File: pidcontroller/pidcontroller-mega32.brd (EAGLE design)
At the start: 100 x 75.4 mm, 26 parts, among them IC2 MAX3232CWE, IC3 MEGA32-A

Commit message: updated board
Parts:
- added BTNDN, BTNOK, BTNUP: (no value), wirepad:2,15/1,0
- added R4, R5, R6: (no value), resistor:R0603
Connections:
- new net BTNDN: BTNDN.1, IC3.12, R5.1
- new net BTNOK: BTNOK.1, IC3.11, R6.1
- new net BTNUP: BTNUP.1, IC3.13, R4.1
- net GND: now also R4.2, R5.2, R6.2
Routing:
- net BTNUP: track 0.00 -> 24.9 mm
- net BTNDN: track 0.00 -> 20.1 mm
- net BTNOK: track 0.00 -> 16.1 mm
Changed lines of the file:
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@@
 <?xml version="1.0" encoding="utf-8"?>
 <!DOCTYPE eagle SYSTEM "eagle.dtd">
-<eagle version="6.4">
+<eagle version="6.5.0">
 <drawing>
 <settings>
@@
 <element name="JP6" library="pinhead" package="1X01" value="" x="21" y="11"/>
 <element name="JP7" library="pinhead" package="1X01" value="" x="21" y="17"/>
+<element name="BTNUP" library="wirepad" package="2,15/1,0" value="" x="39" y="24"/>
+<element name="BTNDN" library="wirepad" package="2,15/1,0" value="" x="39" y="28"/>
+<element name="BTNOK" library="wirepad" package="2,15/1,0" value="" x="39" y="32"/>
+<element name="R4" library="resistor" package="R0603" value="" x="34" y="24" rot="R180"/>
+<element name="R5" library="resistor" package="R0603" value="" x="34" y="28" rot="R180"/>
+<element name="R6" library="resistor" package="R0603" value="" x="34" y="32" rot="R180"/>
 </elements>
 <signals>
@@
 <vertex x="100" y="75"/>
 </polygon>
+<contactref element="R6" pad="2"/>
+<contactref element="R5" pad="2"/>
+<contactref element="R4" pad="2"/>
 </signal>
 <signal name="N$9">
@@
 <contactref element="IC3" pad="14"/>
 <contactref element="R1" pad="2"/>
-<wire x1="50.8" y1="24.218" x2="50.8" y2="29.464" width="0.4064" layer="1"/>
-<wire x1="50.8" y1="29.464" x2="52.21" y2="29.464" width="0.4064" layer="1"/>
-<wire x1="52.21" y1="29.464" x2="52.21" y2="32.3" width="0.4064" layer="1"/>
+<wire x1="52.21" y1="32.3" x2="52.21" y2="24.218" width="0.4064" layer="1"/>
+<wire x1="52.21" y1="24.218" x2="50.8" y2="24.218" width="0.4064" layer="1"/>
 </signal>
 <signal name="N$10">
@@
 <wire x1="31.27" y1="5" x2="31.27" y2="8.46" width="0.4064" layer="1"/>
 </signal>
+<signal name="BTNUP">
+<contactref element="R4" pad="1"/>
+<contactref element="BTNUP" pad="1"/>
+<contactref element="IC3" pad="13"/>
+<wire x1="51.41" y1="32.3" x2="51.41" y2="26" width="0.4064" layer="1"/>
+<wire x1="51.41" y1="26" x2="41" y2="26" width="0.4064" layer="1"/>
+<wire x1="41" y1="26" x2="41" y2="24" width="0.4064" layer="1"/>
+<wire x1="41" y1="24" x2="39" y2="24" width="0.4064" layer="1"/>
+<wire x1="34.85" y1="24" x2="39" y2="24" width="0.4064" layer="1"/>
+</signal>
+<signal name="BTNDN">
+<contactref element="R5" pad="1"/>
+<contactref element="BTNDN" pad="1"/>
+<contactref element="IC3" pad="12"/>
+<wire x1="50.61" y1="32.3" x2="50.61" y2="28" width="0.4064" layer="1"/>
+<wire x1="50.61" y1="28" x2="39" y2="28" width="0.4064" layer="1"/>
+<wire x1="34.85" y1="28" x2="39" y2="28" width="0.4064" layer="1"/>
+</signal>
+<signal name="BTNOK">
+<contactref element="R6" pad="1"/>
+<contactref element="BTNOK" pad="1"/>
+<contactref element="IC3" pad="11"/>
+<wire x1="48.81" y1="34.1" x2="41" y2="34.1" width="0.4064" layer="1"/>
+<wire x1="41" y1="34.1" x2="41" y2="32" width="0.4064" layer="1"/>
+<wire x1="41" y1="32" x2="39" y2="32" width="0.4064" layer="1"/>
+<wire x1="34.85" y1="32" x2="39" y2="32" width="0.4064" layer="1"/>
+</signal>
 </signals>

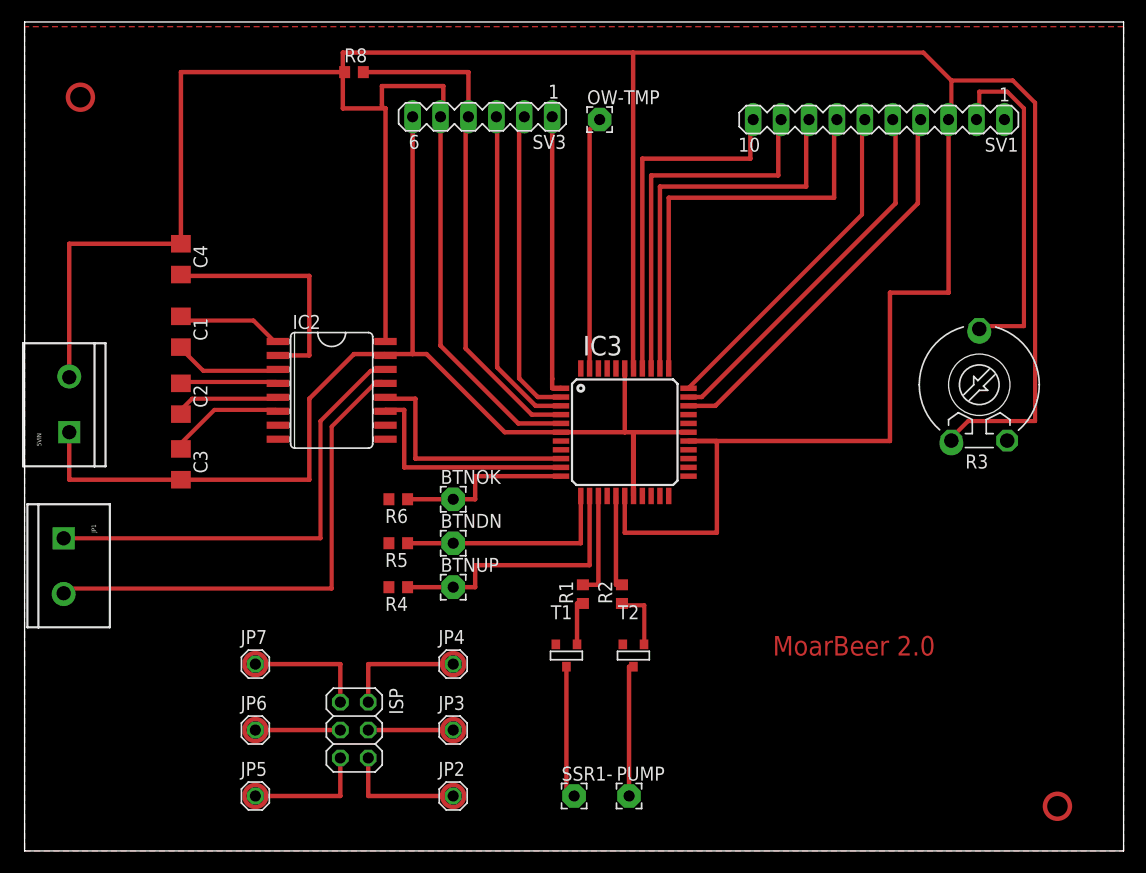
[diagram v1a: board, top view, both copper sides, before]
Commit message: thicker lines
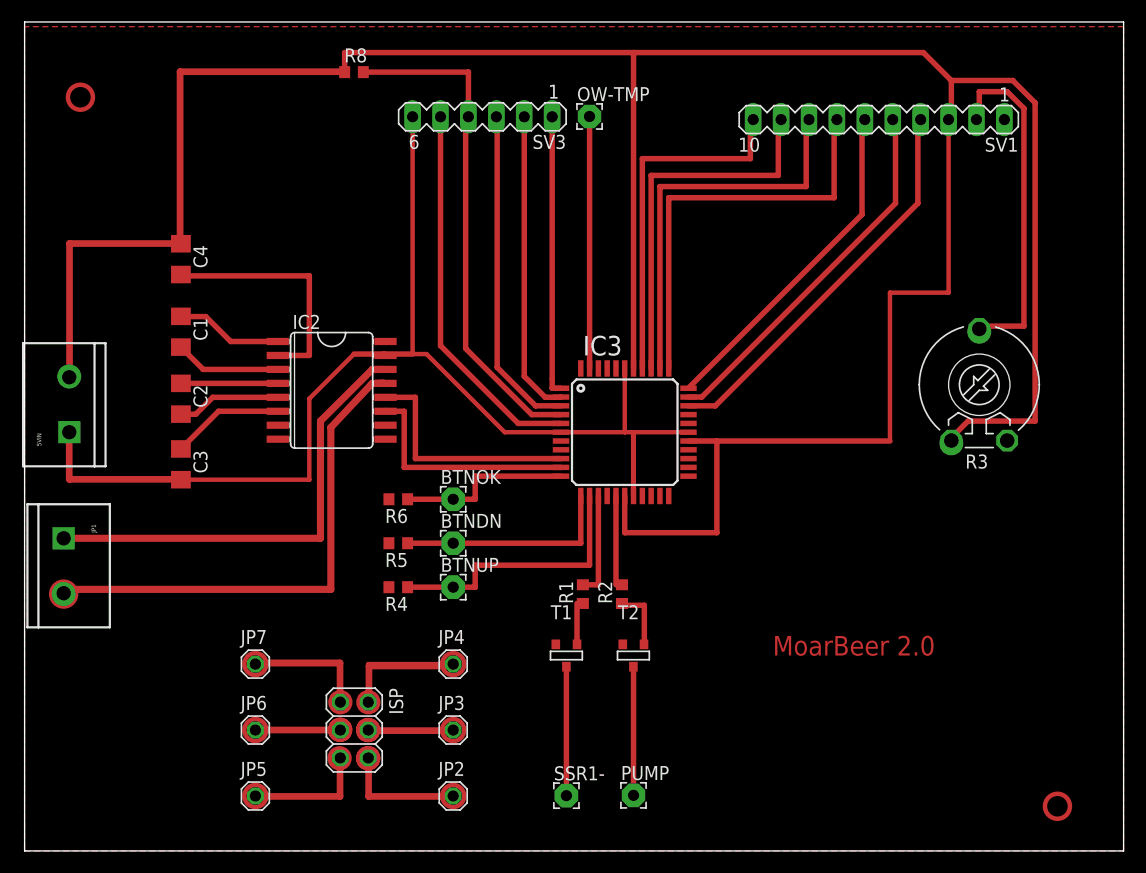
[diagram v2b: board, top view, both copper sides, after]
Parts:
- moved OW-TMP 0.96 mm to (51.4, 66.8)
- moved SSR1- 0.70 mm to (49.3, 5.03)
- moved PUMP 0.41 mm to (55.4, 5.06)
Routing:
- net N$39: track 0.00 -> 45.2 mm
- net VCC: track 339.2 -> 299.7 mm
- net N$30: track 0.00 -> 30.0 mm
- net N$29: track 0.00 -> 22.0 mm
- net N$31: track 0.00 -> 14.1 mm
- net N$37: track 0.00 -> 11.4 mm
- net N$35: track 0.00 -> 11.1 mm
- net N$34: track 0.00 -> 11.1 mm
- net N$32: track 0.00 -> 10.1 mm
- net N$36: track 0.00 -> 7.67 mm
- net N$33: track 0.00 -> 7.55 mm
- net N$15: track 28.5 -> 27.8 mm
- net N$23: track 12.5 -> 11.7 mm

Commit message: changed stuff
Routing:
- net GND: track 111.9 -> 42.1 mm
- net N$39: track 45.2 -> 0.00 mm
- net N$30: track 30.0 -> 0.00 mm
- net N$29: track 22.0 -> 0.00 mm
- net VCC: track 299.7 -> 314.6 mm, vias 1 -> 0
- net N$31: track 14.1 -> 0.00 mm
- net N$37: track 11.4 -> 0.00 mm
- net N$35: track 11.1 -> 0.00 mm
- net N$34: track 11.1 -> 0.00 mm
- net N$32: track 10.1 -> 0.00 mm
- net N$36: track 7.67 -> 0.06 mm
- net N$33: track 7.55 -> 0.00 mm, vias 0 -> 1
- net D7: track 36.2 -> 37.8 mm
- net D5: track 31.2 -> 32.4 mm
- net D6: track 33.9 -> 34.9 mm

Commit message: fixed wire
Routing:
- net GND: track 42.1 -> 27.7 mm
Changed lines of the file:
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@@
 <?xml version="1.0" encoding="utf-8"?>
 <!DOCTYPE eagle SYSTEM "eagle.dtd">
-<eagle version="6.5.0">
+<eagle version="6.6.0">
 <drawing>
 <settings>
@@
 <contactref element="R5" pad="2"/>
 <contactref element="R4" pad="2"/>
-<wire x1="48.81" y1="38.1" x2="42.9963125" y2="38.1" width="0.4064" layer="1"/>
-<wire x1="42.9963125" y1="38.1" x2="37.469834375" y2="43.626478125" width="0.4064" layer="1" curve="-90"/>
-<wire x1="37.469834375" y1="43.626478125" x2="36.761909375" y2="43.626478125" width="0.4064" layer="1"/>
-<wire x1="36.761909375" y1="43.626478125" x2="35.34525625" y2="45.04313125" width="0.4064" layer="1" curve="-90"/>
 <wire x1="35.34525625" y1="45.04313125" x2="32.88406875" y2="45.04313125" width="0.4064" layer="1"/>
 <wire x1="32.88406875" y1="45.04313125" x2="32.8422" y2="45.085" width="0.4064" layer="1" curve="-90"/>
@@
 <wire x1="54.61" y1="38.1" x2="55.41" y2="38.1" width="0.4064" layer="1"/>
 <wire x1="55.41" y1="38.1" x2="55.41" y2="32.3" width="0.4064" layer="1"/>
+<wire x1="48.81" y1="38.1" x2="48.81" y2="38.0482375" width="0.4064" layer="1"/>
+<wire x1="48.81" y1="38.0482375" x2="46.860796875" y2="38.0482375" width="0.4064" layer="1"/>
 </signal>
 <signal name="N$9">

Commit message: changed stuff
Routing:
- net VCC: track 314.6 -> 303.0 mm
- added copper zone on layer 1, net N$38

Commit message: updated isp
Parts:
- removed JP2, JP4: (no value), pinhead:1X01
- moved ISP 47.4 mm to (76.8, 18.6)
- moved JP3 47.4 mm to (85.8, 18.6)
- moved JP5 47.4 mm to (67.8, 12.6)
- moved JP6 47.4 mm to (67.8, 18.6)
- moved JP7 47.4 mm to (67.8, 24.6)
- moved R3 0.23 mm to (86.6, 42.4)
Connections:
- removed net N$21: ISP.6, JP2.1
- removed net N$25: ISP.2, JP4.1
- net GND: now also ISP.6
- net VCC: now also ISP.2
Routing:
- net VCC: track 303.0 -> 236.6 mm
- net N$17: track 31.5 -> 19.1 mm
- net N$25: track 11.2 -> 0.00 mm
- net N$21: track 11.2 -> 0.00 mm

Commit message: updated
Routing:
- net VCC: track 236.6 -> 298.6 mm

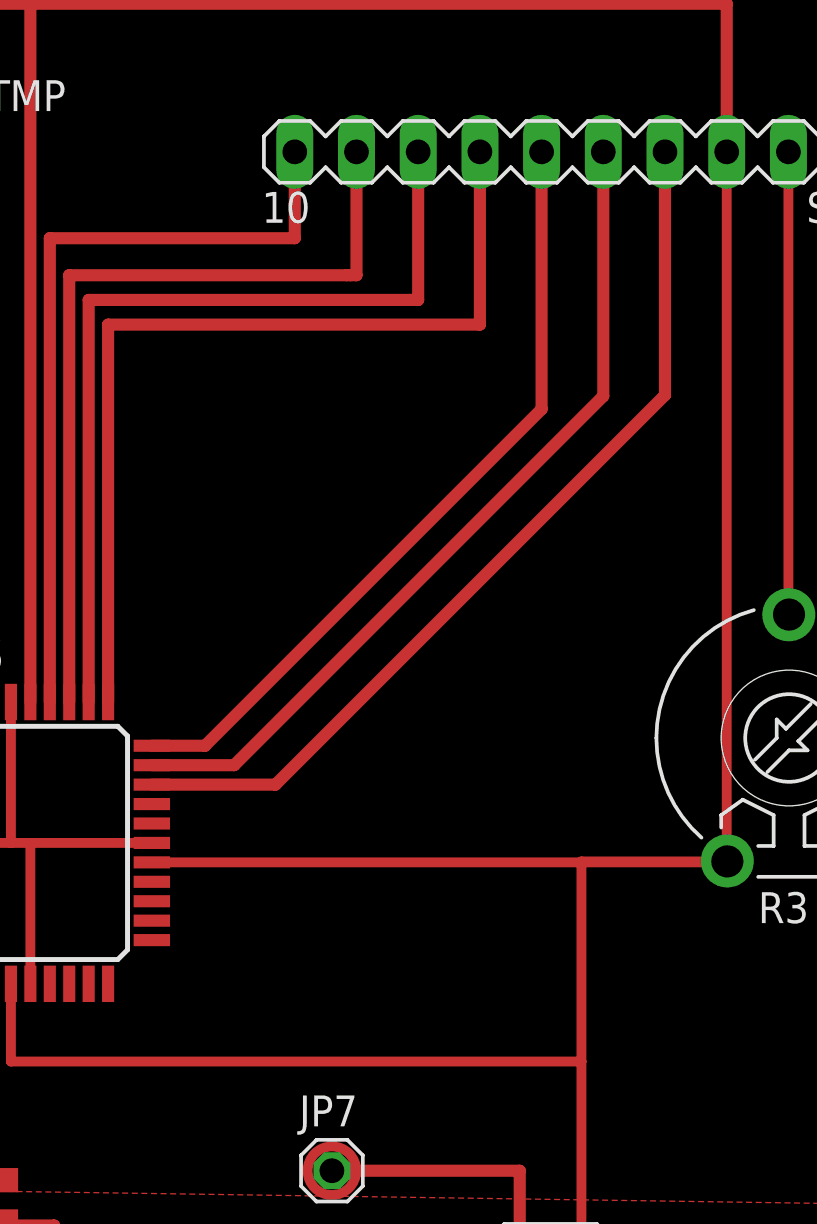
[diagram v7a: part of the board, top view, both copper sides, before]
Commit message: added extra pins
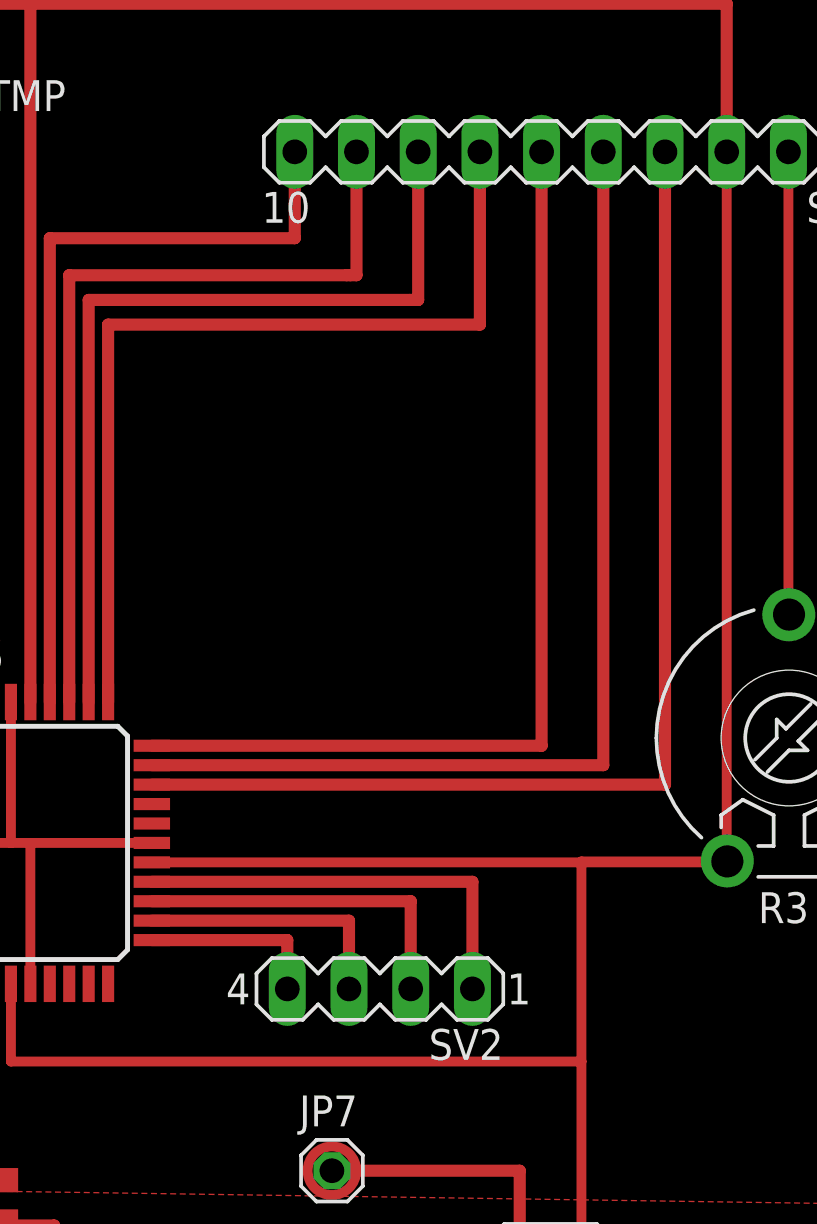
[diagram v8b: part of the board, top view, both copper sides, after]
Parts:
- added SV2: (no value), con-lstb:MA04-1
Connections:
- new net N$40: IC3.26, SV2.1
- new net N$41: IC3.25, SV2.2
- new net N$42: IC3.24, SV2.3
- new net N$43: IC3.23, SV2.4
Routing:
- net N$40: track 0.00 -> 17.6 mm
- net N$41: track 0.00 -> 14.3 mm
- net N$42: track 0.00 -> 10.9 mm
- net D7: track 37.8 -> 47.2 mm
- net D6: track 34.9 -> 43.8 mm
- net D5: track 32.4 -> 40.5 mm
- net N$43: track 0.00 -> 7.59 mm
